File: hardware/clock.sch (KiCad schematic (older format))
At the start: 63 parts, among them U301 ADCMP580, U302 CDCLVP1204, U303 SY89321L-synth_lib, U304 ICS853S057I, U305 X0060L5050AHF, X301 DV75D-010.0M

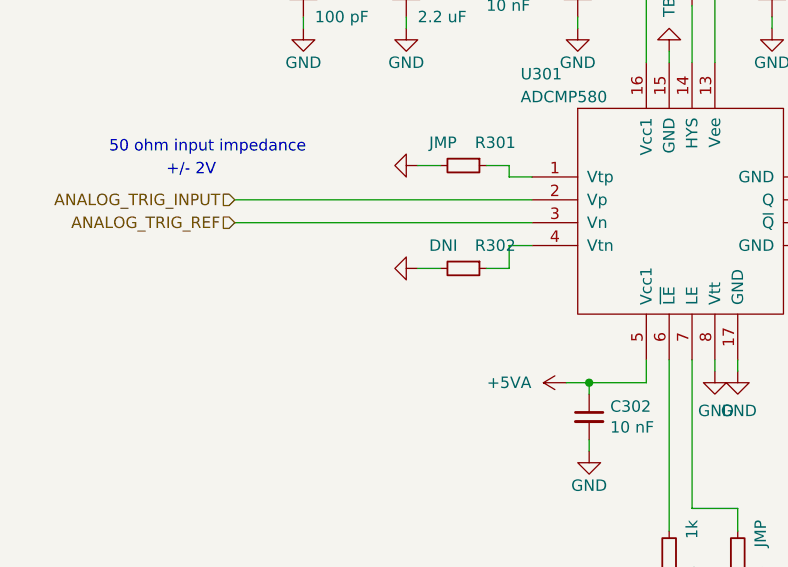
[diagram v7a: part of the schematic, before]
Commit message: more layout.. 28 unrouted nets to go
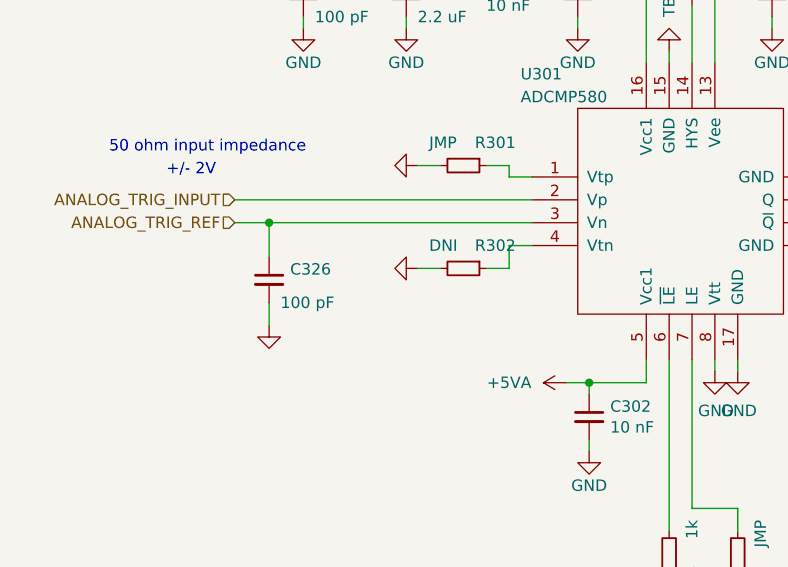
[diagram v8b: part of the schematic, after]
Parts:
- added C326: 100 pF, Capacitors_SMD:C_0402, symbol Device:C_Small
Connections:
- net ANALOG_TRIG_REF: now also C326.1
- net GND: now also C326.2
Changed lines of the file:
@@
 	1300 6750 2600 6750
 Wire Wire Line
-	1300 6850 2600 6850
+	1300 6850 1450 6850
 Text HLabel 1300 6850 0    50   Input ~ 0
 ANALOG_TRIG_REF
@@
 Wire Wire Line
 	8250 4800 8550 4800
+$Comp
+L Device:C_Small C326
+U 1 1 5C3128F4
+P 1450 7100
+F 0 "C326" H 1542 7146 50  0000 L CNN
+F 1 "100 pF" H 1500 7000 50  0000 L CNN
+F 2 "Capacitors_SMD:C_0402" H 1450 7100 50  0001 C CNN
+F 3 "~" H 1450 7100 50  0001 C CNN
+	1    1450 7100
+	1    0    0    -1
+$EndComp
+$Comp
+L power:GND #PWR?
+U 1 1 5C3129B8
+P 1450 7300
+AR Path="/5BC41CC8/5C3129B8" Ref="#PWR?"  Part="1"
+AR Path="/5BC3F72A/5C3129B8" Ref="#PWR0154"  Part="1"
+F 0 "#PWR0154" H 1450 7050 50  0001 C CNN
+F 1 "GND" V 1500 7300 50  0001 C CNN
+F 2 "" H 1450 7300 50  0001 C CNN
+F 3 "" H 1450 7300 50  0001 C CNN
+	1    1450 7300
+	1    0    0    -1
+$EndComp
+Wire Wire Line
+	1450 7200 1450 7300
+Wire Wire Line
+	1450 7000 1450 6850
+Connection ~ 1450 6850
+Wire Wire Line
+	1450 6850 2600 6850
 $EndSCHEMATC
